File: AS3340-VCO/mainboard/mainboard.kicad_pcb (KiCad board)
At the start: 2 copper layers, 34.9 x 107.9 mm, 82 parts, among them J1 Conn_02x05_Odd_Even, J2 Conn_01x03, J3 Conn_02x05_Odd_Even, Q1 Q_NPN_EBC, Q2 Q_NPN_EBC, U1 TL071, U2 TL074, U3 AS3340, U4 TL074

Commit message: Add -5V regulator so internal zener doesn't heat up
The internal zener of the AS3340 chip will heat up the chip, causing it
to take ~45 minutes to create a stable frequency. With an external -5V
it only takes 15 minutes.
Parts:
- removed REF** (x2): MountingHole_3.2mm_M3_NoCourt, Library:MountingHole_3.2mm_M3_NoCourt
- added C14: 100nF, Capacitor_SMD:C_0603_1608Metric_Pad1.08x0.95mm_HandSolder, F.Cu at (102.2, 87.2)
- added C15: 100nF, Capacitor_SMD:C_0603_1608Metric_Pad1.08x0.95mm_HandSolder, F.Cu at (101.2, 89.7)
- added U5: L7905, Package_TO_SOT_SMD:SOT-89-3_Handsoldering, F.Cu at (106.6, 88.0)
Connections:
- net /VEE renamed -5V
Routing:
- net -5V: track 17.9 -> 40.9 mm, vias 1 -> 3
- net -12V: track 227.3 -> 243.6 mm, vias 5 -> 6
- net GND: track 76.2 -> 78.5 mm
- net /HARD_SYNC: track 67.6 -> 68.6 mm
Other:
- board text added: "no R15 if 7905 is present!->"

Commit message: Finish DuinoRack hardware, final touches on AS3340 VCO
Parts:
- removed RV_SCALE1: 10k, Potentiometer_THT:Potentiometer_Bourns_3266Y_Vertical
- added C16: 560p, Capacitor_SMD:C_0603_1608Metric_Pad1.08x0.95mm_HandSolder, F.Cu at (109.2, 98.6)
- added C17: 100nF, Capacitor_SMD:C_0603_1608Metric_Pad1.08x0.95mm_HandSolder, F.Cu at (115.8, 142.5)
- added C18: 100nF, Capacitor_SMD:C_0603_1608Metric_Pad1.08x0.95mm_HandSolder, F.Cu at (112.9, 147.0)
- added H1: MountingHole, Library:MountingHole_3.2mm_M3_NoCourt, F.Cu at (116.0, 135.5)
- added J4: TP1, Connector_PinHeader_2.54mm:PinHeader_1x01_P2.54mm_Vertical, B.Cu at (86.7, 95.0)
- added J5: TP2, Connector_PinHeader_2.54mm:PinHeader_1x01_P2.54mm_Vertical, B.Cu at (86.7, 89.9)
- added JP1: SET_REF_PITCH, Connector_PinHeader_2.54mm:PinHeader_1x02_P2.54mm_Vertical, B.Cu at (98.2, 87.7)
- added R51: 1k6, Resistor_SMD:R_0603_1608Metric_Pad0.98x0.95mm_HandSolder, F.Cu at (117.1, 94.6)
- added R52: 1k, Resistor_SMD:R_0603_1608Metric_Pad0.98x0.95mm_HandSolder, F.Cu at (115.5, 86.3)
- added R53: 100k, Resistor_SMD:R_0603_1608Metric_Pad0.98x0.95mm_HandSolder, F.Cu at (112.1, 89.0)
- added R54: 100k, Resistor_SMD:R_0603_1608Metric_Pad0.98x0.95mm_HandSolder, F.Cu at (112.0, 86.3)
- added R55: 1k, Resistor_SMD:R_0603_1608Metric_Pad0.98x0.95mm_HandSolder, F.Cu at (114.3, 140.9)
- added R56: 100k, Resistor_SMD:R_0603_1608Metric_Pad0.98x0.95mm_HandSolder, F.Cu at (115.7, 147.1)
- added R57: 100k, Resistor_SMD:R_0603_1608Metric_Pad0.98x0.95mm_HandSolder, F.Cu at (109.7, 149.5)
- added R58: 470k, Resistor_SMD:R_0603_1608Metric_Pad0.98x0.95mm_HandSolder, F.Cu at (118.1, 122.5)
- added REFIND_C6: 100k, Potentiometer_THT:Potentiometer_Bourns_3266Y_Vertical, B.Cu at (109.3, 84.9)
- added REF_PITCH_C6: 10k, Potentiometer_THT:Potentiometer_Bourns_3266Y_Vertical, B.Cu at (108.1, 121.6)
- added SCALE_ADJ1: 500, Potentiometer_THT:Potentiometer_Bourns_3266Y_Vertical, B.Cu at (114.5, 93.2)
- added TEMPCO_ADJ1: 5k, Potentiometer_THT:Potentiometer_Bourns_3266Y_Vertical, B.Cu at (90.1, 89.6)
- added TP1: 7V, Connector_PinHeader_2.54mm:PinHeader_1x01_P2.54mm_Vertical, B.Cu at (116.6, 150.4)
- added TP2: 1V, Connector_PinHeader_2.54mm:PinHeader_1x01_P2.54mm_Vertical, B.Cu at (116.2, 122.2)
- added TRIM_1V1: 200k, Potentiometer_THT:Potentiometer_Bourns_3266Y_Vertical, B.Cu at (116.5, 130.8)
- added TRIM_7V1: 100k, Potentiometer_THT:Potentiometer_Bourns_3266Y_Vertical, B.Cu at (112.3, 144.5)
- added U6: TL431DBZ, Package_TO_SOT_SMD:SOT-23, F.Cu at (112.5, 149.5)
- J1: value Conn_02x05_Odd_Even -> Conn_02x06_Odd_Even; footprint Connector_PinHeader_2.54mm:PinHeader_2x05_P2.54mm_Vertical -> Connector_PinHeader_2.54mm:PinHeader_2x06_P2.54mm_Vertical
- J2: value Conn_01x03 -> Conn_01x04; footprint Connector_PinHeader_2.54mm:PinHeader_1x03_P2.54mm_Vertical -> Connector_PinHeader_2.54mm:PinHeader_1x04_P2.54mm_Vertical
- R11: value 1.5M -> 1.3M *
- R17: value 24k -> 18k
- R19: value 1.8k -> 22k
- R21: value 820 -> 5.6k
- R4: value 300k -> 220k
- U5: value L7905 -> TL431DBZ; footprint Package_TO_SOT_SMD:SOT-89-3_Handsoldering -> Package_TO_SOT_SMD:SOT-23
- moved R19 19.8 mm to (112.2, 118.3)
- moved C13 3.16 mm to (116.2, 153.6)
- moved J1 1.00 mm to (105.1, 61.7)
- moved C15 0.32 mm to (101.6, 89.7)
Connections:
- C14 pad 2: -12V -> -5V
- C4 pad 1: GND -> /CAP
- C4 pad 2: Net-(C4-Pad2) -> GND
- C9 pad 2: -12V -> GND
- R11 pad 1: +12V -> Net-(R11-Pad1)
- R19 pad 1: GND -> Net-(R19-Pad1)
- R19 pad 2: Net-(R19-Pad2) -> GND
- R21 pad 2: -12V -> Net-(J4-Pad1)
- R4 pad 1: +12V -> Net-(R4-Pad1)
- U3 pad 11: Net-(C4-Pad2) -> /CAP
- U3 pad 14: Net-(R19-Pad2) -> Net-(C16-Pad1)
- U5 pad 2: -12V -> Net-(R53-Pad2)
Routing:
- net GND: track 78.5 -> 147.0 mm, vias 11 -> 18
- net /CAP: track 0.00 -> 63.4 mm, vias 0 -> 1
- net /+1.000V: track 0.00 -> 62.6 mm
- net -12V: track 243.6 -> 189.3 mm, vias 6 -> 5
- net /+7.000V: track 0.00 -> 42.4 mm, vias 0 -> 1
- net Net-(R11-Pad1): track 0.00 -> 36.8 mm, vias 0 -> 2
- net Net-(C16-Pad1): track 0.00 -> 29.1 mm, vias 0 -> 1
- net Net-(J4-Pad1): track 0.00 -> 19.5 mm, vias 0 -> 1
- net Net-(J5-Pad1): track 2.59 -> 17.2 mm, vias 0 -> 2
- net Net-(R53-Pad2): track 0.00 -> 10.4 mm
- net Net-(R56-Pad2): track 0.00 -> 7.41 mm
- net Net-(R4-Pad1): track 0.00 -> 6.87 mm, vias 0 -> 1
- net +12V: track 224.3 -> 228.9 mm, vias 5 -> 6
- net Net-(R24-Pad2): track 46.8 -> 50.8 mm
- net /OFFSET: track 86.7 -> 83.0 mm
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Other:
- board text added: "TL431"
- board text removed: "no R15 if 7905 is present!->"

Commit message: Saving latest changes
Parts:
- added TP3: GND, Connector_PinHeader_2.54mm:PinHeader_1x01_P2.54mm_Vertical, B.Cu at (114.8, 114.7)
- J4: value TP1 -> TEMP1
- J5: value TP2 -> TEMP2
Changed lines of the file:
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@@
   (net 74 "Net-(R51-Pad2)")
   (net 75 "Net-(R56-Pad1)")
-  (net 76 "Net-(TRIM_1V1-Pad3)")
+  (net 76 "Net-(R58-Pad1)")
   (footprint "Resistor_SMD:R_0603_1608Metric_Pad0.98x0.95mm_HandSolder" (layer "F.Cu")
     (at 109.29 80.42 180)
@@
     (fp_line (start 0.8 -0.4125) (end 0.8 0.4125) (layer "F.Fab") (width 0.1))
     (pad "1" smd roundrect (at -0.9125 0 90) (size 0.975 0.95) (layers "F.Cu" "F.Paste" "F.Mask") (roundrect_rratio 0.25)
-      (net 76 "Net-(TRIM_1V1-Pad3)") (pintype "passive"))
+      (net 76 "Net-(R58-Pad1)") (pintype "passive"))
     (pad "2" smd roundrect (at 0.9125 0 90) (size 0.975 0.95) (layers "F.Cu" "F.Paste" "F.Mask") (roundrect_rratio 0.25)
       (net 68 "/+1.000V") (pintype "passive"))
@@
     )
   )
+  (footprint "Connector_PinHeader_2.54mm:PinHeader_1x01_P2.54mm_Vertical" (layer "B.Cu")
+    (at 114.85 114.68 180)
+    (descr "Through hole straight pin header, 1x01, 2.54mm pitch, single row")
+    (tags "Through hole pin header THT 1x01 2.54mm single row")
+    (property "Sheetfile" "mainboard.kicad_sch")
+    (property "Sheetname" "")
+    (attr through_hole)
+    (fp_text reference "TP3" (at 0 2.33) (layer "B.SilkS")
+      (effects (font (size 1 1) (thickness 0.15)) (justify mirror))
+    )
+    (fp_text value "GND" (at -2.5 -0.05 90) (layer "B.SilkS")
+      (effects (font (size 1 1) (thickness 0.15)) (justify mirror))
+    )
+    (fp_text user "${REFERENCE}" (at 0 0 90) (layer "B.Fab")
+      (effects (font (size 1 1) (thickness 0.15)) (justify mirror))
+    )
+    (fp_line (start -1.33 1.33) (end 0 1.33) (layer "B.SilkS") (width 0.12))
+    (fp_line (start 1.33 -1.27) (end 1.33 -1.33) (layer "B.SilkS") (width 0.12))
+    (fp_line (start -1.33 -1.27) (end -1.33 -1.33) (layer "B.SilkS") (width 0.12))
+    (fp_line (start -1.33 0) (end -1.33 1.33) (layer "B.SilkS") (width 0.12))
+    (fp_line (start -1.33 -1.27) (end 1.33 -1.27) (layer "B.SilkS") (width 0.12))
+    (fp_line (start -1.33 -1.33) (end 1.33 -1.33) (layer "B.SilkS") (width 0.12))
+    (fp_line (start -1.8 -1.8) (end 1.8 -1.8) (layer "B.CrtYd") (width 0.05))
+    (fp_line (start -1.8 1.8) (end -1.8 -1.8) (layer "B.CrtYd") (width 0.05))
+    (fp_line (start 1.8 1.8) (end -1.8 1.8) (layer "B.CrtYd") (width 0.05))
+    (fp_line (start 1.8 -1.8) (end 1.8 1.8) (layer "B.CrtYd") (width 0.05))
+    (fp_line (start -1.27 0.635) (end -0.635 1.27) (layer "B.Fab") (width 0.1))
+    (fp_line (start 1.27 -1.27) (end -1.27 -1.27) (layer "B.Fab") (width 0.1))
+    (fp_line (start 1.27 1.27) (end 1.27 -1.27) (layer "B.Fab") (width 0.1))
+    (fp_line (start -1.27 -1.27) (end -1.27 0.635) (layer "B.Fab") (width 0.1))
+    (fp_line (start -0.635 1.27) (end 1.27 1.27) (layer "B.Fab") (width 0.1))
+    (pad "1" thru_hole rect (at 0 0 180) (size 1.7 1.7) (drill 1) (layers *.Cu *.Mask)
+      (net 4 "GND") (pinfunction "1") (pintype "passive"))
+    (model "${KICAD6_3DMODEL_DIR}/Connector_PinHeader_2.54mm.3dshapes/PinHeader_1x01_P2.54mm_Vertical.wrl"
+      (offset (xyz 0 0 0))
+      (scale (xyz 1 1 1))
+      (rotate (xyz 0 0 0))
+    )
+  )
   (footprint "Potentiometer_THT:Potentiometer_Bourns_3266Y_Vertical" (layer "B.Cu")
     (at 112.26 144.54 180)
@@
       (net 34 "/+7.000V") (pinfunction "2") (pintype "passive"))
     (pad "3" thru_hole circle (at -5.08 0 270) (size 1.44 1.44) (drill 0.8) (layers *.Cu *.Mask)
-      (net 76 "Net-(TRIM_1V1-Pad3)") (pinfunction "3") (pintype "passive"))
+      (net 76 "Net-(R58-Pad1)") (pinfunction "3") (pintype "passive"))
     (model "${KICAD6_3DMODEL_DIR}/Potentiometer_THT.3dshapes/Potentiometer_Bourns_3266Y_Vertical.wrl"
       (offset (xyz 0 0 0))
@@
       (effects (font (size 1 1) (thickness 0.15)) (justify mirror))
     )
-    (fp_text value "TP1" (at 0.46 -2.39) (layer "B.SilkS")
+    (fp_text value "TEMP1" (at 0.23 -2.24) (layer "B.SilkS")
       (effects (font (size 0.8 0.8) (thickness 0.15)) (justify mirror))
     )
@@
       (effects (font (size 1 1) (thickness 0.15)) (justify mirror))
     )
-    (fp_text value "TP2" (at 0.43 2.36) (layer "B.SilkS")
+    (fp_text value "TEMP2" (at 0.12 2.4) (layer "B.SilkS")
       (effects (font (size 0.8 0.8) (thickness 0.15)) (justify mirror))
     )
@@
     (property "Sheetname" "")
     (attr through_hole)
-    (fp_text reference "TEMPCO_ADJ1" (at -2.54 3.41) (layer "B.SilkS")
+    (fp_text reference "TEMPCO_ADJ1" (at -2.7 7.72 90) (layer "B.SilkS")
       (effects (font (size 1 1) (thickness 0.15)) (justify mirror))
     )

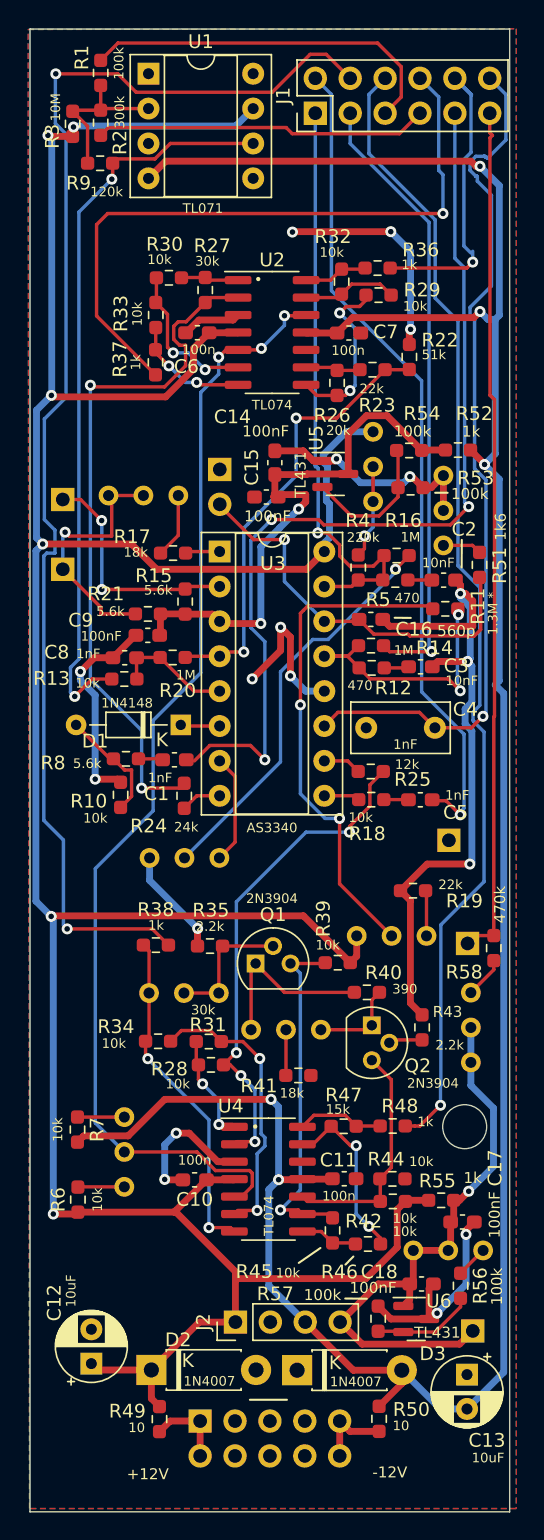
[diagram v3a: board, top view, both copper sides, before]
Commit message: Apply rev1 fixes to AS3340 VCO
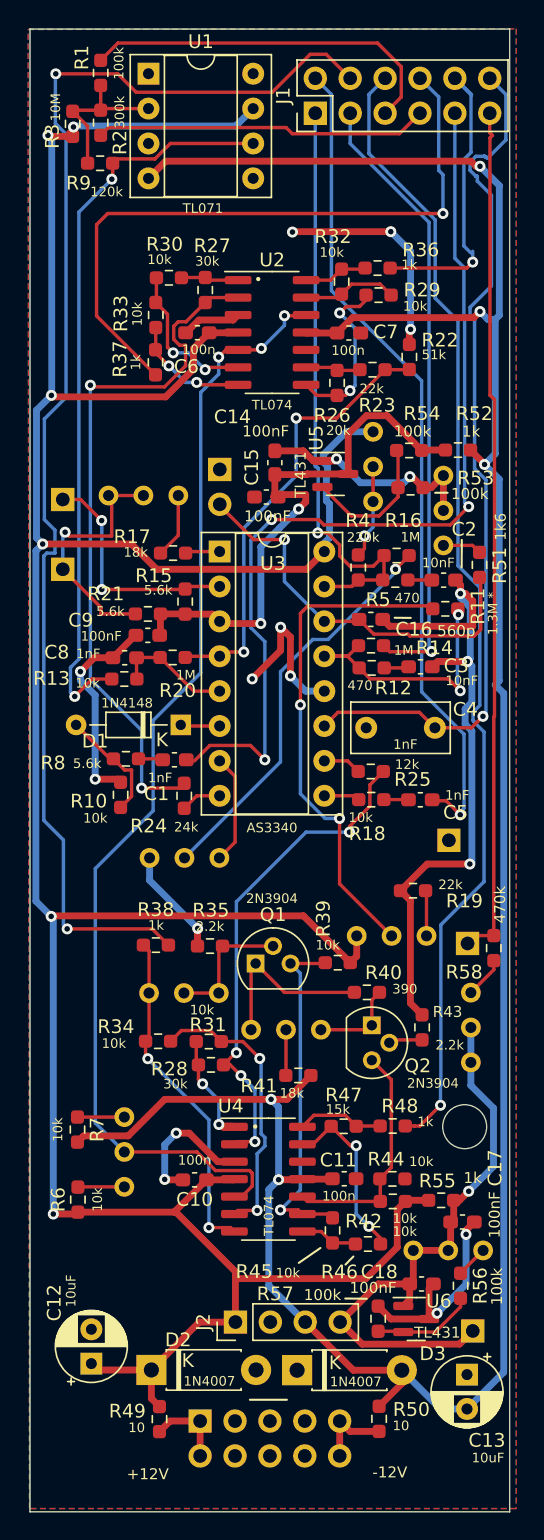
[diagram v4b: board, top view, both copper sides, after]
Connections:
- R41 pad 2: GND -> -12V
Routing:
- net -12V: track 189.3 -> 192.9 mm
